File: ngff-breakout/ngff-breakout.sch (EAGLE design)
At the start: 79 parts, among them U2 LD1085D2T33R, X1 PINHD-2X4, X3 694108106102, X8 ZX360D-B-10P(30), Y1 MHF4, Y2 MHF4, Y3 MHF4

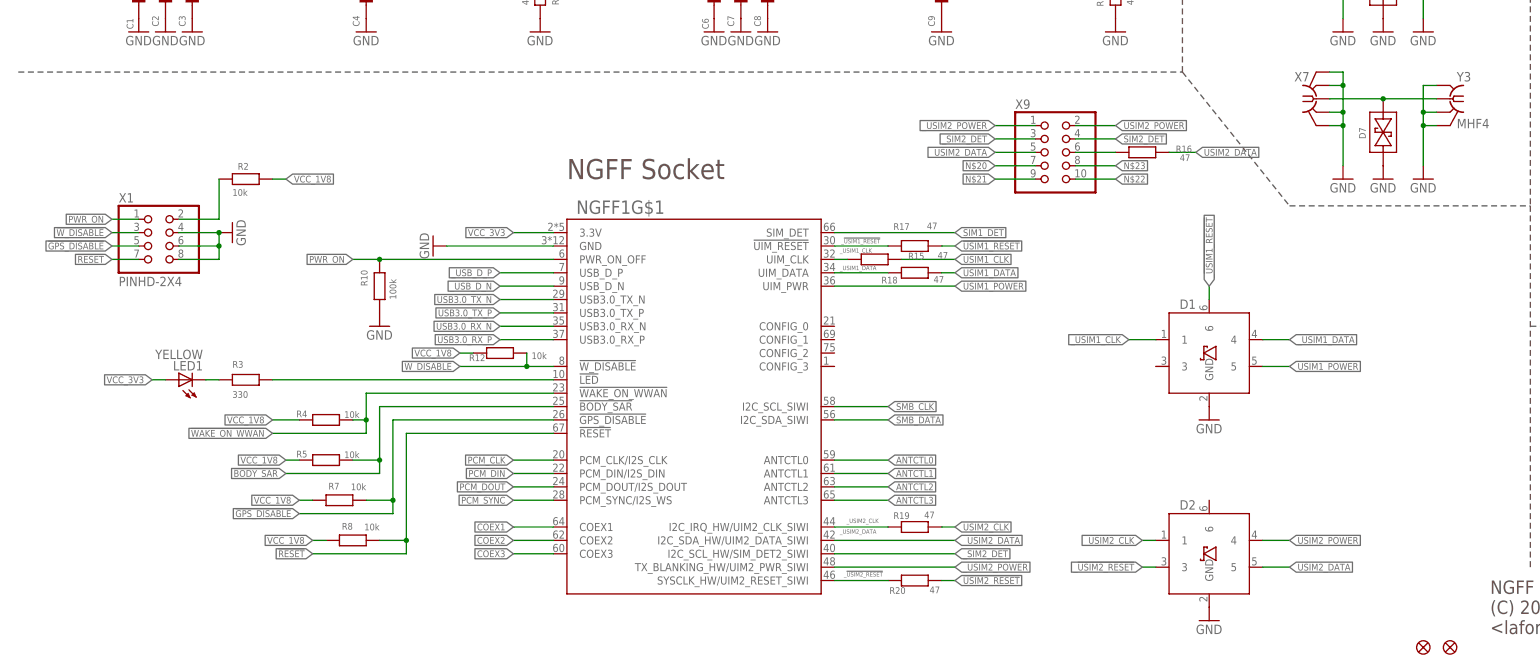
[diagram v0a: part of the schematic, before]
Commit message: ngff: 2/2 make room for 2x5 header and route SIM2 signals there
...and run ERC/DRC

adresses OS#4211
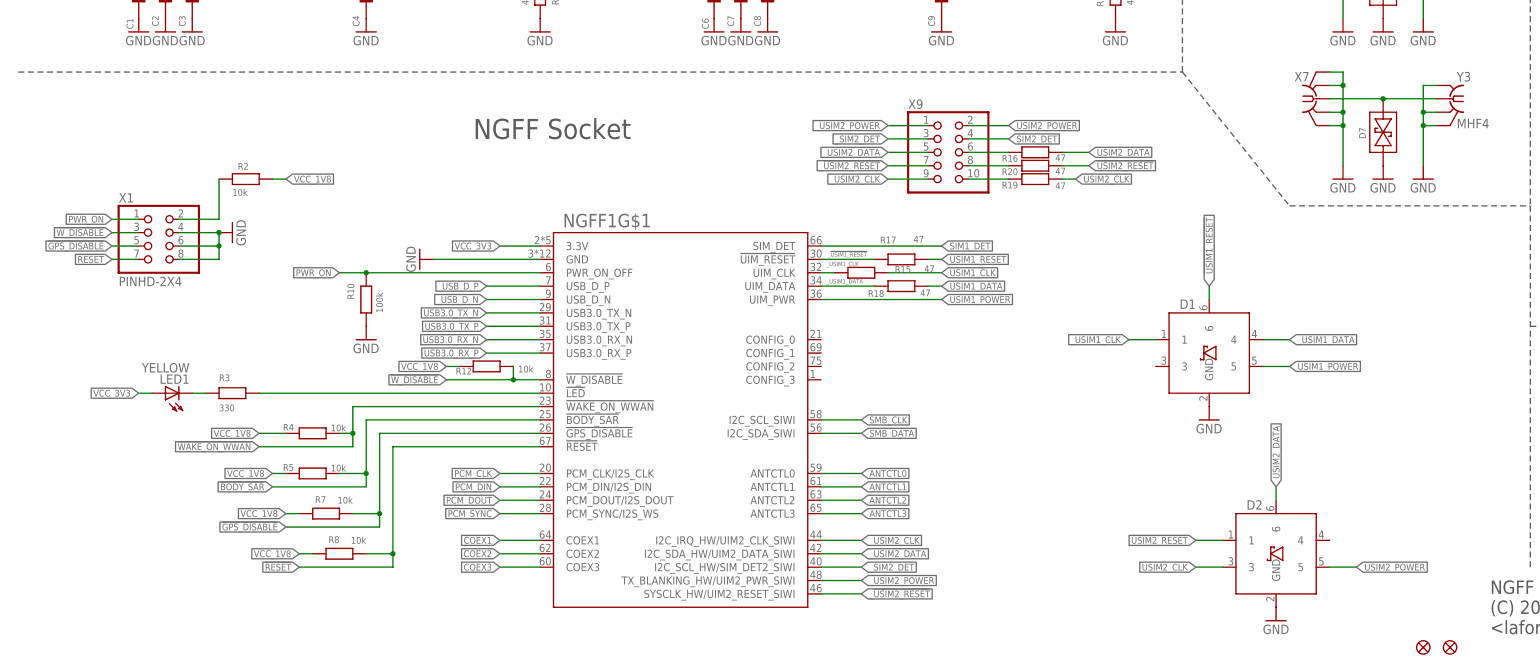
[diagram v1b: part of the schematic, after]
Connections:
- removed net N$20: X9.7
- removed net N$21: X9.9
- removed net N$22: X9.10
- removed net N$23: X9.8
- new net N$16: R20.1, X9.8
- new net N$19: R19.1, X9.10
- net !USIM2_RESET: now also D2.1
- net USIM2_CLK: now also D2.3
- net USIM2_DATA: now also D2.6; no longer D2.5
- net USIM2_POWER: now also D2.5; no longer D2.4
- net _!USIM2_RESET: now also X9.7; no longer D2.3, R20.1
- net _USIM2_CLK: now also X9.9; no longer D2.1, R19.1
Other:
- moved on the sheet: D2, LED1, NGFF1G$1, R10, R12, R15, R16, R17, R18, R19, R20, R3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

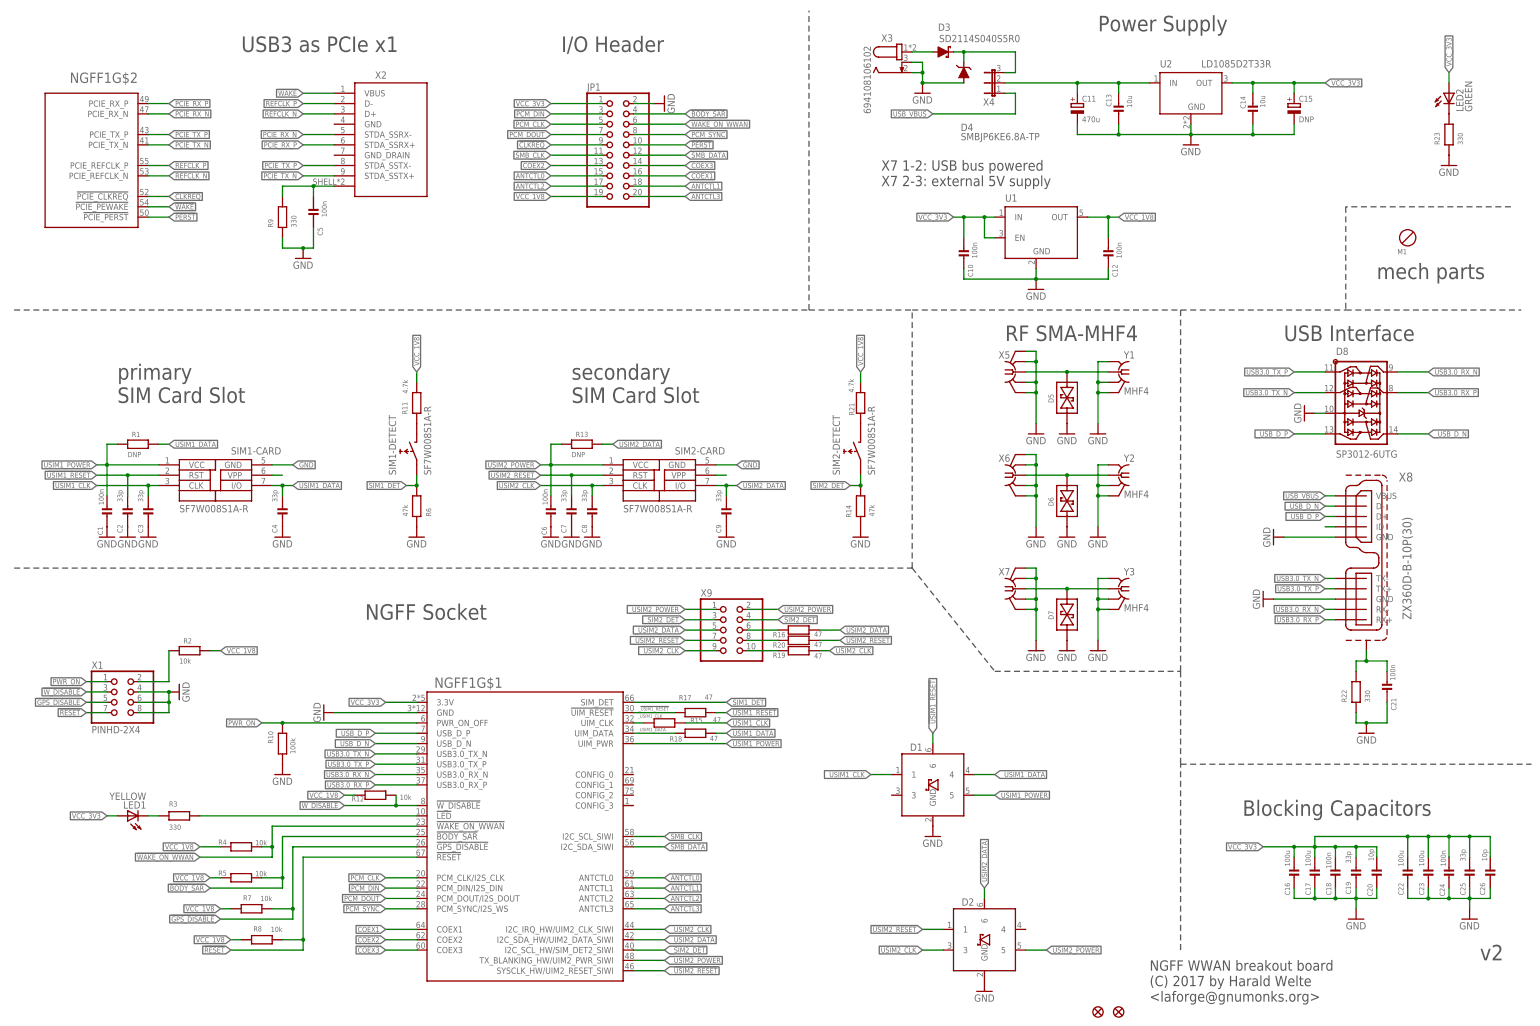
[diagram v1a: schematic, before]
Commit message: ngff: re-introduce and re-position OSHW logo and bott silk screen
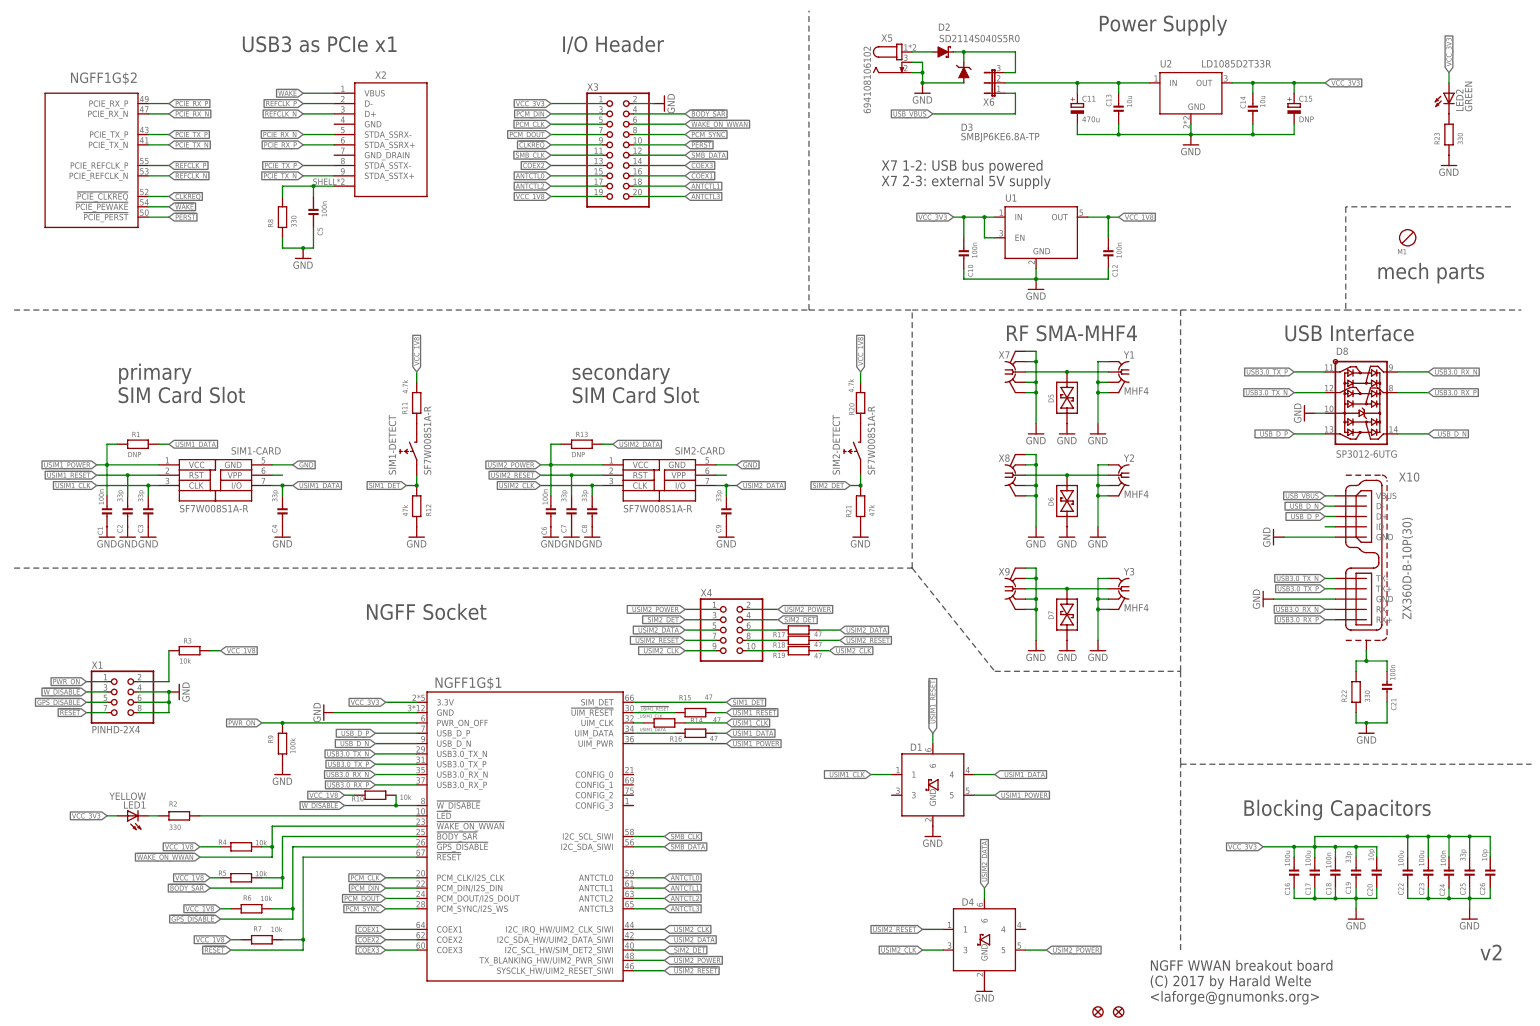
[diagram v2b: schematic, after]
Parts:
- removed JP3: FIDUCIALUFIDUCIAL, SparkFun:FIDUCIALUFIDUCIAL
- added X10: ZX360D-B-10P(30), USB30-MICROB:USB3.0-MICROB
- D2: value PESD5V0UBV -> SD2114S040S5R0; device laforge:PESD5V0UBV -> diodes-sysmocom:DIODE-SCHOTTKY-SMB; DESCRIPTION TVS DIODE 5V SOT666 -> DIODE SCHOTTKY 40V 5A SMB; LINK https://www.digikey.de/product-detail/de/nexperia-usa-inc/P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 -> https://www.digikey.de/product-detail/de/avx-corporation/SD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; MANUFACTURER Nexperia USA Inc. -> AVX Corporation; MANUFACTURERPARTNUMBER PESD5V0U5BV,115 -> SD2114S040S5R0; ROHSCERTIFICATE Bleifrei / RoHS3-konform -> UNKNOWN ROHS CERTIFICATE; SOURCEPARTNUMBER 1727-5806-1-ND -> 478-7816-1-ND
- D3: value SD2114S040S5R0 -> SMBJP6KE6.8A-TP; device diodes-sysmocom:DIODE-SCHOTTKY-SMB -> diodes-sysmocom:DIODE-TVS-SMB; DESCRIPTION DIODE SCHOTTKY 40V 5A SMB -> TVS DIODE 5.8V 10.5V DO214AA; LINK https://www.digikey.de/product-detail/de/avx-corporation/SD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 -> https://www.digikey.de/product-detail/de/micro-commercial-c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; MANUFACTURER AVX Corporation -> Micro Commercial Co; MANUFACTURERPARTNUMBER SD2114S040S5R0 -> SMBJP6KE6.8A-TP; ROHSCERTIFICATE UNKNOWN ROHS CERTIFICATE -> Bleifrei / RoHS-konform; SOURCEPARTNUMBER 478-7816-1-ND -> SMBJP6KE6.8A-TPMSCT-ND
- D4: value SMBJP6KE6.8A-TP -> PESD5V0UBV; device diodes-sysmocom:DIODE-TVS-SMB -> laforge:PESD5V0UBV; DESCRIPTION TVS DIODE 5.8V 10.5V DO214AA -> TVS DIODE 5V SOT666; LINK https://www.digikey.de/product-detail/de/micro-commercial-c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 -> https://www.digikey.de/product-detail/de/nexperia-usa-inc/P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; MANUFACTURER Micro Commercial Co -> Nexperia USA Inc.; MANUFACTURERPARTNUMBER SMBJP6KE6.8A-TP -> PESD5V0U5BV,115; ROHSCERTIFICATE Bleifrei / RoHS-konform -> Bleifrei / RoHS3-konform; SOURCEPARTNUMBER SMBJP6KE6.8A-TPMSCT-ND -> 1727-5806-1-ND
- JP1: value (none) -> FIDUCIALUFIDUCIAL; device laforge:PINHD-2X10 -> SparkFun:FIDUCIALUFIDUCIAL; POPULATED TRUE -> FALSE
- R10: value 100k -> 10k; DESCRIPTION RES SMD 100K OHM 1%% 1/10W 0603 -> RES 10K OHM 1%% 1/10W 0603; LINK https://www.digikey.de/product-detail/de/vishay-dale/CRCW06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 -> https://www.digikey.de/product-detail/de/stackpole-electron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; MANUFACTURER Vishay Dale -> Stackpole Electronics Inc; MANUFACTURERPARTNUMBER CRCW0603100KFKEA -> RMCF0603FT10K0; ROHSCERTIFICATE Bleifrei / RoHS-konform -> UNKNOWN ROHS CERTIFICATE; SOURCEPARTNUMBER 541-100KHCT-ND -> RMCF0603FT10K0CT-ND
- R12: value 10k -> 47k; DESCRIPTION RES 10K OHM 1%% 1/10W 0603 -> RES 47K OHM 1%% 1/10W 0603; LINK https://www.digikey.de/product-detail/de/stackpole-electronics-inc/RMCF0603FT10K0/RMCF0603FT10K0CT-ND -> https://www.digikey.de/product-detail/de/stackpole-electronics-inc/RMCF0603FT47K0/RMCF0603FT47K0CT-ND; MANUFACTURERPARTNUMBER RMCF0603FT10K0 -> RMCF0603FT47K0; ROHSCERTIFICATE UNKNOWN ROHS CERTIFICATE -> Bleifrei / RoHS-konform; SOURCEPARTNUMBER RMCF0603FT10K0CT-ND -> RMCF0603FT47K0CT-ND
- R14: value 47k -> 47; device rc-sysmocom:RESISTOR_0603 -> rc-sysmocom:RESISTOR_0402; DESCRIPTION RES 47K OHM 1%% 1/10W 0603 -> RES SMD 47 OHM 5%% 1/10W 0603; LINK https://www.digikey.de/product-detail/de/stackpole-electron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 -> http://www.digikey.de/product-detail/de/yageo/RC0603JR-0747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; MANUFACTURER Stackpole Electronics Inc -> Yageo; MANUFACTURERPARTNUMBER RMCF0603FT47K0 -> RC0603JR-0747RL; SOURCEPARTNUMBER RMCF0603FT47K0CT-ND -> 311-47GRCT-ND
- R15: DESCRIPTION RES SMD 47 OHM 5%% 1/10W 0603 -> CRGCQ 0402 47R 1%%; LINK http://www.digikey.de/product-detail/de/yageo/RC0603JR-0747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 -> https://www.digikey.de/product-detail/de/te-connectivity-pa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; MANUFACTURER Yageo -> TE Connectivity Passive Product; MANUFACTURERPARTNUMBER RC0603JR-0747RL -> CRGCQ0402F47R; ROHSCERTIFICATE Bleifrei / RoHS-konform -> UNKNOWN ROHS CERTIFICATE; SOURCEPARTNUMBER 311-47GRCT-ND -> A129611CT-ND
- R17: DESCRIPTION CRGCQ 0402 47R 1%% -> RES SMD 47 OHM 5%% 1/10W 0603; LINK https://www.digikey.de/product-detail/de/te-connectivity-pa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 -> http://www.digikey.de/product-detail/de/yageo/RC0603JR-0747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; MANUFACTURER TE Connectivity Passive Product -> Yageo; MANUFACTURERPARTNUMBER CRGCQ0402F47R -> RC0603JR-0747RL; ROHSCERTIFICATE UNKNOWN ROHS CERTIFICATE -> Bleifrei / RoHS-konform; SOURCEPARTNUMBER A129611CT-ND -> 311-47GRCT-ND
- R2, R8: value 10k -> 330; DESCRIPTION RES 10K OHM 1%% 1/10W 0603 -> RES SMD 330 OHM 5%% 1/10W 0603; LINK https://www.digikey.de/product-detail/de/stackpole-electron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 -> http://www.digikey.de/product-detail/de/yageo/RC0603JR-0733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; MANUFACTURER Stackpole Electronics Inc -> Yageo; MANUFACTURERPARTNUMBER RMCF0603FT10K0 -> RC0603JR-07330RL; ROHSCERTIFICATE UNKNOWN ROHS CERTIFICATE -> Bleifrei / RoHS-konform; SOURCEPARTNUMBER RMCF0603FT10K0CT-ND -> 311-330GRCT-ND
- R20: value 47 -> 4.7k; device rc-sysmocom:RESISTOR_0402 -> rc-sysmocom:RESISTOR_0603; DESCRIPTION RES SMD 47 OHM 5%% 1/10W 0603 -> RES SMD 4.7K OHM 5% 1/10W 0603; LINK http://www.digikey.de/product-detail/de/yageo/RC0603JR-0747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 -> http://www.digikey.de/product-detail/de/RC0603JR-074K7L/311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; MANUFACTURERPARTNUMBER RC0603JR-0747RL -> RC0603JR-074K7L; SOURCEPARTNUMBER 311-47GRCT-ND -> 311-4.7KGRCT-ND
- R21: value 4.7k -> 47k; DESCRIPTION RES SMD 4.7K OHM 5% 1/10W 0603 -> RES 47K OHM 1%% 1/10W 0603; LINK http://www.digikey.de/product-detail/de/RC0603JR-074K7L/311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 -> https://www.digikey.de/product-detail/de/stackpole-electron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; MANUFACTURER Yageo -> Stackpole Electronics Inc; MANUFACTURERPARTNUMBER RC0603JR-074K7L -> RMCF0603FT47K0; SOURCEPARTNUMBER 311-4.7KGRCT-ND -> RMCF0603FT47K0CT-ND
- R3: value 330 -> 10k; DESCRIPTION RES SMD 330 OHM 5%% 1/10W 0603 -> RES 10K OHM 1%% 1/10W 0603; LINK http://www.digikey.de/product-detail/de/yageo/RC0603JR-0733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 -> https://www.digikey.de/product-detail/de/stackpole-electron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; MANUFACTURER Yageo -> Stackpole Electronics Inc; MANUFACTURERPARTNUMBER RC0603JR-07330RL -> RMCF0603FT10K0; ROHSCERTIFICATE Bleifrei / RoHS-konform -> UNKNOWN ROHS CERTIFICATE; SOURCEPARTNUMBER 311-330GRCT-ND -> RMCF0603FT10K0CT-ND
- R6: value 47k -> 10k; DESCRIPTION RES 47K OHM 1%% 1/10W 0603 -> RES 10K OHM 1%% 1/10W 0603; LINK https://www.digikey.de/product-detail/de/stackpole-electronics-inc/RMCF0603FT47K0/RMCF0603FT47K0CT-ND -> https://www.digikey.de/product-detail/de/stackpole-electronics-inc/RMCF0603FT10K0/RMCF0603FT10K0CT-ND; MANUFACTURERPARTNUMBER RMCF0603FT47K0 -> RMCF0603FT10K0; ROHSCERTIFICATE Bleifrei / RoHS-konform -> !DOCTYPE HTML PUBLIC "-//W3C//DTD HTML 4.01//EN" "http://ww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; SOURCEPARTNUMBER RMCF0603FT47K0CT-ND -> RMCF0603FT10K0CT-ND
- R7: ROHSCERTIFICATE !DOCTYPE HTML PUBLIC "-//W3C//DTD HTML 4.01//EN" "http://ww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 -> UNKNOWN ROHS CERTIFICATE
- R9: value 330 -> 100k; DESCRIPTION RES SMD 330 OHM 5%% 1/10W 0603 -> RES SMD 100K OHM 1%% 1/10W 0603; LINK http://www.digikey.de/product-detail/de/yageo/RC0603JR-0733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 -> https://www.digikey.de/product-detail/de/vishay-dale/CRCW06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; MANUFACTURER Yageo -> Vishay Dale; MANUFACTURERPARTNUMBER RC0603JR-07330RL -> CRCW0603100KFKEA; SOURCEPARTNUMBER 311-330GRCT-ND -> 541-100KHCT-ND
- X3: value 694108106102 -> (none); device Wurth_Elektronik_Electromechanic_DC_Power_Jack_Connectors_rev15c:694108106102 -> laforge:PINHD-2X10; CLASS RELAY -> CONNECTOR\JUMPER; DESCRIPTION CONN PWR JACK 2.5X5.5MM SOLDER -> NO DESCRIPTION; LINK http://www.digikey.de/product-detail/de/wurth-electronics-i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 -> UNKNOWN LINK; MANUFACTURER Wurth Electronics Inc. -> UNKNOWN MANUFACTURER; MANUFACTURERPARTNUMBER 694108106102 -> UNKNOWN MANUFACTURER PART NUMBER; ROHSCERTIFICATE Bleifrei / RoHS-konform -> UNKNOWN ROHS CERTIFICATE; SOURCE DIGIKEY -> UNKNOWN SOURCE; SOURCEPARTNUMBER 732-5933-1-ND -> UNKNOWN SOURCE PART NUMBER
- X4: device jumper:JP2E -> laforge:PINHD-2X5; CLASS CONNECTOR\JUMPER -> (none); DESCRIPTION NO DESCRIPTION -> (none); LINK UNKNOWN LINK -> (none); MANUFACTURER UNKNOWN MANUFACTURER -> (none); MANUFACTURERPARTNUMBER UNKNOWN MANUFACTURER PART NUMBER -> (none); POPULATED TRUE -> (none); ROHSCERTIFICATE UNKNOWN ROHS CERTIFICATE -> (none); SOURCE UNKNOWN SOURCE -> (none); SOURCEPARTNUMBER UNKNOWN SOURCE PART NUMBER -> (none)
- X5: value (none) -> 694108106102; device laforge:SMA-F-S-TH -> Wurth_Elektronik_Electromechanic_DC_Power_Jack_Connectors_rev15c:694108106102; CLASS CONNECTOR -> RELAY; DESCRIPTION CONN SMA JACK STR 50 OHM PCB -> CONN PWR JACK 2.5X5.5MM SOLDER; LINK http://www.digikey.de/product-detail/de/te-connectivity-amp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 -> http://www.digikey.de/product-detail/de/wurth-electronics-i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; MANUFACTURER TE Connectivity AMP Connectors -> Wurth Electronics Inc.; MANUFACTURERPARTNUMBER 5-1814832-1 -> 694108106102; SOURCEPARTNUMBER A97594-ND -> 732-5933-1-ND
- X6: device laforge:SMA-F-S-TH -> jumper:JP2E; CLASS CONNECTOR -> CONNECTOR\JUMPER; DESCRIPTION CONN SMA JACK STR 50 OHM PCB -> NO DESCRIPTION; LINK http://www.digikey.de/product-detail/de/te-connectivity-amp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 -> UNKNOWN LINK; MANUFACTURER TE Connectivity AMP Connectors -> UNKNOWN MANUFACTURER; MANUFACTURERPARTNUMBER 5-1814832-1 -> UNKNOWN MANUFACTURER PART NUMBER; ROHSCERTIFICATE Bleifrei / RoHS-konform -> UNKNOWN ROHS CERTIFICATE; SOURCE DIGIKEY -> UNKNOWN SOURCE; SOURCEPARTNUMBER A97594-ND -> UNKNOWN SOURCE PART NUMBER
- X8: value ZX360D-B-10P(30) -> (none); device USB30-MICROB:USB3.0-MICROB -> laforge:SMA-F-S-TH; CLASS CAPACITOR -> CONNECTOR; DESCRIPTION CONN RCPT USB3.0 MICRO B SMD R/A -> CONN SMA JACK STR 50 OHM PCB; LINK https://www.digikey.de/product-detail/de/hirose-electric-co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 -> http://www.digikey.de/product-detail/de/te-connectivity-amp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; MANUFACTURER Hirose Electric Co Ltd -> TE Connectivity AMP Connectors; MANUFACTURERPARTNUMBER ZX360D-B-10P(30) -> 5-1814832-1; SOURCEPARTNUMBER H125269DKR-ND -> A97594-ND
- X9: device laforge:PINHD-2X5 -> laforge:SMA-F-S-TH; CLASS (none) -> CONNECTOR; DESCRIPTION (none) -> CONN SMA JACK STR 50 OHM PCB; LINK (none) -> http://www.digikey.de/product-detail/de/te-connectivity-amp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; MANUFACTURER (none) -> TE Connectivity AMP Connectors; MANUFACTURERPARTNUMBER (none) -> 5-1814832-1; POPULATED (none) -> TRUE; ROHSCERTIFICATE (none) -> Bleifrei / RoHS-konform; SOURCE (none) -> DIGIKEY; SOURCEPARTNUMBER (none) -> A97594-ND
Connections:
- net !BODY_SAR: now also X3.4; no longer JP1.4
- net !CLKREQ: now also X3.9; no longer JP1.9
- net !GPS_DISABLE: now also R6.1; no longer R7.1
- net !PERST: now also X3.10; no longer JP1.10
- net !RESET: now also R7.1; no longer R8.1
- net !USIM1_RESET: now also R15.2; no longer R17.2
- net !USIM2_RESET: now also D4.1, R18.2; no longer D2.1, R20.2
- net !WAKE_ON_WWAN: now also X3.6; no longer JP1.6
- net !W_DISABLE: now also R10.1; no longer R12.1
- net ANTCTL0: now also X3.15; no longer JP1.15
- net ANTCTL1: now also X3.18; no longer JP1.18
- net ANTCTL2: now also X3.17; no longer JP1.17
- net ANTCTL3: now also X3.20; no longer JP1.20
- net COEX1: now also X3.16; no longer JP1.16
- net COEX2: now also X3.13; no longer JP1.13
- net COEX3: now also X3.14; no longer JP1.14
- net GND: now also D3.A, D4.GND, R12.1, R21.1, R8.1, X10.GND@0, X10.GND@1, X5.2, X5.3, X8.GND@2, X8.GND@3, X8.GND@4, X9.GND@1, X9.GND@2, X9.GND@3, X9.GND@4; no longer D2.GND, D4.A, JP1.2, R10.1, R14.1, R6.1, X3.3, X5.GND@1, X5.GND@2, X5.GND@3, X5.GND@4, X6.GND@1, X6.GND@2, X6.GND@3, X6.GND@4, X8.GND@0
- net LDO_IN: now also X6.2; no longer X4.2
- net N$10: now also X10.S1; no longer X8.S1
- net N$11: now also R20.2; no longer R21.2
- net N$12: now also D2.C, X6.3; no longer D4.C, X4.3
- net N$13: now also X7.1; no longer X5.1
- net N$14: now also X8.1; no longer X6.1
- net N$15: now also R17.1, X4.6; no longer R16.1, X9.6
- net N$16: now also R18.1, X4.8; no longer R20.1, X9.8
- net N$17: now also X10.ID; no longer X8.ID
- net N$18: now also R3.1; no longer R2.1
- net N$19: now also X4.10; no longer X9.10
- net N$2: now also R2.1; no longer R3.1
- net N$3: now also D2.A, X5.1; no longer D3.A, X3.1
- net N$4: now also R8.2; no longer R9.2
- net N$6: now also R2.2; no longer R3.2
- net N$7: now also X9.1; no longer X7.1
- net PCM_CLK: now also X3.5; no longer JP1.5
- net PCM_DIN: now also X3.3; no longer JP1.3
- net PCM_DOUT: now also X3.7; no longer JP1.7
- net PCM_SYNC: now also X3.8; no longer JP1.8
- net PWR_ON: now also R9.2; no longer R10.2
- net SIM1_DET: now also R12.2; no longer R6.2
- net SIM2_DET: now also R21.2, X4.4; no longer R14.2, X9.4
- net SMB_CLK: now also X3.11; no longer JP1.11
- net SMB_DATA: now also X3.12; no longer JP1.12
- net USB3.0_RX_N: now also X10.RX-; no longer X8.RX-
- net USB3.0_RX_P: now also X10.RX+; no longer X8.RX+
- net USB3.0_TX_N: now also X10.TX-; no longer X8.TX-
- net USB3.0_TX_P: now also X10.TX+; no longer X8.TX+
- net USB_VBUS: now also X10.VBUS, X6.1; no longer X4.1, X8.VBUS
- net USIM1_CLK: now also R14.2; no longer R15.2
- net USIM1_DATA: now also R16.2; no longer R18.2
- net USIM2_CLK: now also D4.3; no longer D2.3
- net USIM2_DATA: now also D4.6, R17.2; no longer D2.6, R16.2
- net USIM2_POWER: now also D4.5, X4.2; no longer D2.5, X9.2
- net VCC_1V8: now also R10.2, R20.1, R3.2, R6.2, X3.19; no longer JP1.19, R12.2, R2.2, R21.1, R8.2
- net VCC_3V3: now also X3.1; no longer JP1.1
- net _!USIM1_RESET: now also R15.1; no longer R17.1
- net _!USIM2_RESET: now also X4.7; no longer X9.7
- net _SIM2_DET: now also X4.3; no longer X9.3
- net _USB_D_N: now also X10.D-; no longer X8.D-
- net _USB_D_P: now also X10.D+; no longer X8.D+
- net _USIM1_CLK: now also R14.1; no longer R15.1
- net _USIM1_DATA: now also R16.1; no longer R18.1
- net _USIM2_CLK: now also X4.9; no longer X9.9
- net _USIM2_DATA: now also X4.5; no longer X9.5
- net _USIM2_POWER: now also X4.1; no longer X9.1
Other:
- moved on the sheet: R10, R12, R14, R15, R16, R17, R18, R2, R20, R21, R3, R6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

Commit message: ngff: add / refresh most ext'd attribs for eBOM
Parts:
- D2: MANUFACTURERPARTNUMBER SD2114S040S5R0 -> YPE HTML PUBLIC; ROHSCERTIFICATE UNKNOWN ROHS CERTIFICATE -> Bleifrei / RoHS3-konform
- D8: MANUFACTURERPARTNUMBER SP3012-06UTG -> YPE HTML PUBLIC; ROHSCERTIFICATE UNKNOWN ROHS CERTIFICATE -> Bleifrei / RoHS3-konform
- NGFF1: CLASS UNKNOWN CLASS -> CONNECTOR\JUMPER; DESCRIPTION NO DESCRIPTION -> CONN FEMALE 67POS 0.020 GOLD; MANUFACTURER UNKNOWN MANUFACTURER -> TE Connectivity AMP Connectors; MANUFACTURERPARTNUMBER UNKNOWN MANUFACTURER PART NUMBER -> YPE HTML PUBLIC; ROHSCERTIFICATE UNKNOWN ROHS CERTIFICATE -> Bleifrei / RoHS-konform; SOURCE UNKNOWN SOURCE -> DIGIKEY; SOURCEPARTNUMBER UNKNOWN SOURCE PART NUMBER -> A115899CT-ND
- R1, R10, R13, R3, R4, R5, R7: MANUFACTURERPARTNUMBER RMCF0603FT10K0 -> YPE HTML PUBLIC; ROHSCERTIFICATE UNKNOWN ROHS CERTIFICATE -> Bleifrei / RoHS3-konform
- R14, R16, R17, R18, R19: DESCRIPTION RES SMD 47 OHM 5%% 1/10W 0603 -> RES SMD 47R 0402 1%; LINK http://www.digikey.de/product-detail/de/yageo/RC0603JR-0747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 -> https://www.digikey.de/product-detail/de/te-connectivity-pa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; MANUFACTURER Yageo -> TE Connectivity Passive Product; MANUFACTURERPARTNUMBER RC0603JR-0747RL -> CRGCQ0402F47R; SOURCEPARTNUMBER 311-47GRCT-ND -> A129611CT-ND
- R15: DESCRIPTION CRGCQ 0402 47R 1%% -> RES SMD 47R 0402 1%; LINK https://www.digikey.de/product-detail/de/te-connectivity-passive-product/CRGCQ0402F47R/A129611CT-ND/ -> https://www.digikey.de/product-detail/de/te-connectivity-passive-product/CRGCQ0402F47R/A129611CT-ND; ROHSCERTIFICATE UNKNOWN ROHS CERTIFICATE -> Bleifrei / RoHS-konform
- SIM1, SIM2: CLASS UNKNOWN CLASS -> SIM HOLDER
- U1: value (none) -> MIC5366-1.8YC5; DESCRIPTION NO DESCRIPTION -> IC REG LINEAR 1.8V 150MA SC70-5; LINK UNKNOWN LINK -> https://www.digikey.de/product-detail/de/microchip-technolo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; MANUFACTURER UNKNOWN MANUFACTURER -> Microchip Technology; MANUFACTURERPARTNUMBER UNKNOWN MANUFACTURER PART NUMBER -> MIC5366-1.8YC5-TR; ROHSCERTIFICATE UNKNOWN ROHS CERTIFICATE -> Bleifrei / RoHS3-konform; SOURCE UNKNOWN SOURCE -> DIGIKEY; SOURCEPARTNUMBER UNKNOWN SOURCE PART NUMBER -> 576-3203-1-ND
- U2: value LD1085D2T33R -> MCP1827S-3302E/EB; DESCRIPTION IC REG LINEAR 3.3V 3A D2PAK -> IC REG LINEAR 3.3V 1.5A 3DDPAK; LINK http://www.digikey.de/product-detail/de/stmicroelectronics/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 -> https://www.digikey.de/product-detail/de/microchip-technolo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; MANUFACTURER STMicroelectronics -> Microchip Technology; MANUFACTURERPARTNUMBER LD1085D2T33R -> YPE HTML PUBLIC; ROHSCERTIFICATE Bleifrei / RoHS-konform -> Bleifrei / RoHS3-konform; SOURCEPARTNUMBER 497-1222-1-ND -> MCP1827S-3302E/EB-ND
- X10: CLASS CAPACITOR -> CONNECTOR\JUMPER
- X2: value (none) -> 692121030100; DESCRIPTION NO DESCRIPTION -> CONN RCPT USB3.0 TYPEA 9POS R/A; LINK UNKNOWN LINK -> https://www.digikey.de/product-detail/de/wurth-electronics-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; MANUFACTURER UNKNOWN MANUFACTURER -> Wurth Electronics Inc.; MANUFACTURERPARTNUMBER UNKNOWN MANUFACTURER PART NUMBER -> YPE HTML PUBLIC; ROHSCERTIFICATE UNKNOWN ROHS CERTIFICATE -> Bleifrei / RoHS3-konform; SOURCE UNKNOWN SOURCE -> DIGIKEY; SOURCEPARTNUMBER UNKNOWN SOURCE PART NUMBER -> 732-3146-1-ND
- X3: value (none) -> PINHD-2X10
- X4: value (none) -> PINHD-2X5; CLASS (none) -> CONNECTOR\JUMPER; DESCRIPTION (none) -> NO DESCRIPTION; LINK (none) -> UNKNOWN LINK; MANUFACTURER (none) -> UNKNOWN MANUFACTURER; MANUFACTURERPARTNUMBER (none) -> UNKNOWN MANUFACTURER PART NUMBER; POPULATED (none) -> TRUE; ROHSCERTIFICATE (none) -> UNKNOWN ROHS CERTIFICATE; SOURCE (none) -> UNKNOWN SOURCE; SOURCEPARTNUMBER (none) -> UNKNOWN SOURCE PART NUMBER
- X5: CLASS RELAY -> CONNECTOR\JUMPER
- X6: value (none) -> PINHD-1X3
- X7, X8, X9: value (none) -> 5-1814832-1; CLASS CONNECTOR -> CONNECTOR\JUMPER
- Y1, Y2, Y3: CLASS CONNECTOR -> CONNECTOR\JUMPER; MANUFACTURERPARTNUMBER MM4829-2702RA4 -> YPE HTML PUBLIC; ROHSCERTIFICATE UNKNOWN ROHS CERTIFICATE -> Bleifrei / RoHS3-konform
